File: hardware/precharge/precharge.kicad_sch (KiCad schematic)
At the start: 14 parts

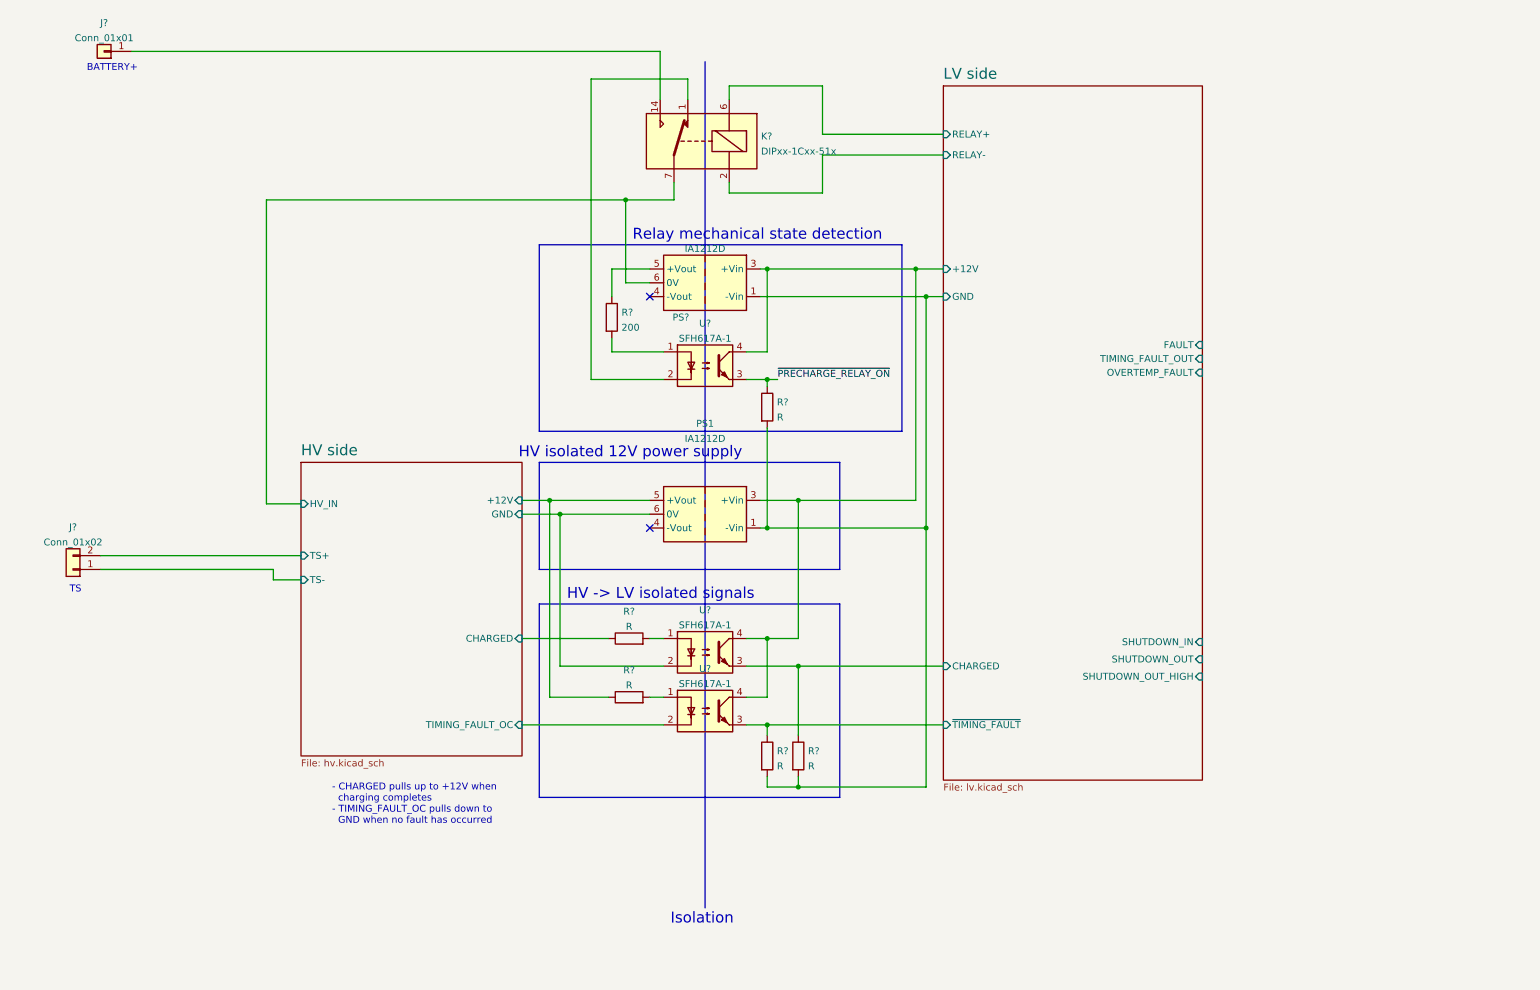
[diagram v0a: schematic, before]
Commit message: Added part numbers for most components, added LEDs, tweaked LV side.
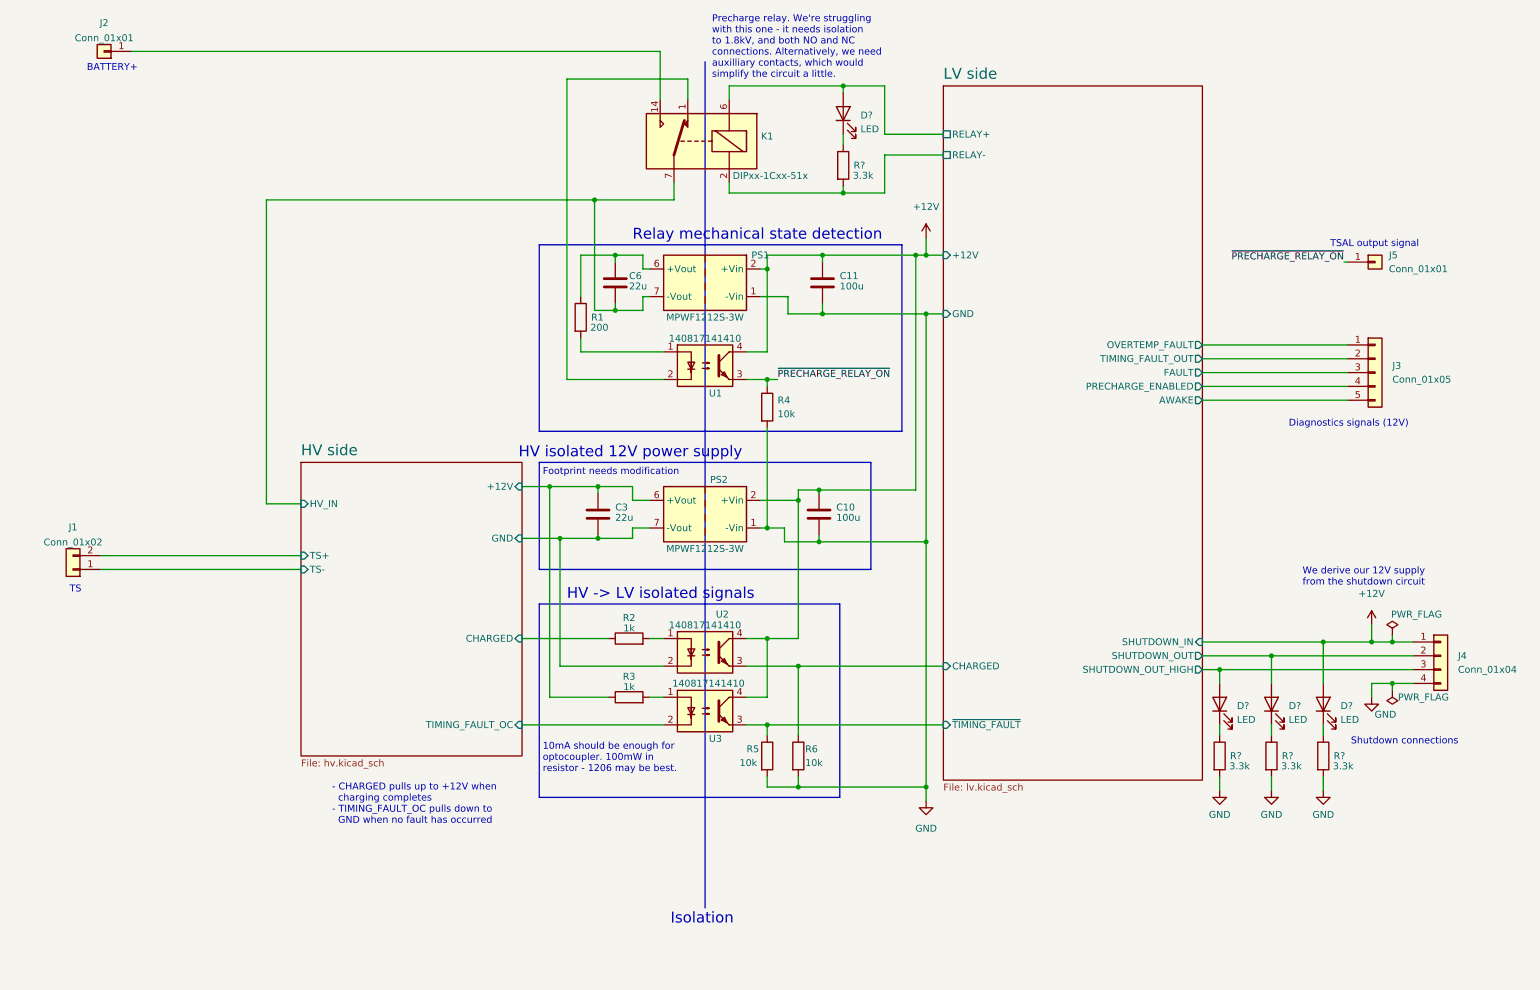
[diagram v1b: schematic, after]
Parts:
- removed PS1, PS?: IA1212D, Converter_DCDC:Converter_DCDC_XP_POWER-IAxxxxD_THT, symbol Converter_DCDC:IA1212D
- added C10, C11: 100u, symbol Device:C
- added C3, C6: 22u, symbol Device:C
- added D? (x4): LED, symbol Device:LED
- added J3: Conn_01x05, symbol Connector_Generic:Conn_01x05
- added J4: Conn_01x04, symbol Connector_Generic:Conn_01x04
- added J5: Conn_01x01, symbol Connector_Generic:Conn_01x01
- added PS1, PS2: MPWF1212S-3W, Converter_DCDC:Converter_DCDC_XP_POWER-ITXxxxxSA_THT, symbol Converter_DCDC:ITX1212SA
- added R? (x4): 3.3k, symbol Device:R
- R2, R3: renamed from R?; value R -> 1k
- R4, R5, R6: renamed from R?; value R -> 10k
- U1, U2, U3: renamed from U?; value SFH617A-1 -> 140817141410
- gave numbers to parts that had none: 4
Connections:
- net HV side/+12V: now also C3.2, PS2.6 (+Vout)
- net HV side/GND: now also C3.1, PS2.7 (-Vout)
- net HV side/HV_IN: now also C6.1, PS1.7 (-Vout)
- net LV side/FAULT: now also J3.3 (Pin_3)
- net LV side/OVERTEMP_FAULT: now also J3.1 (Pin_1)
- net LV side/RELAY+: now also D?.2 (A)
- net LV side/RELAY-: now also R?.2
- net LV side/SHUTDOWN_OUT: now also D?.2 (A), J4.2 (Pin_2)
- net LV side/SHUTDOWN_OUT_HIGH: now also D?.2 (A), J4.3 (Pin_3)
- net LV side/TIMING_FAULT_OUT: now also J3.2 (Pin_2)
- net ~{PRECHARGE_RELAY_ON}: now also J5.1 (Pin_1)
- net at R1.1: now also C6.2, PS1.6 (+Vout)
- net LV side/+12V renamed +12V
- net +12V: now also C10.2, C11.2, D?.2 (A), J4.1 (Pin_1), PS1.2 (+Vin), PS2.2 (+Vin)
- net LV side/GND renamed GND
- net GND: now also C10.1, C11.1, J4.4 (Pin_4), PS1.1 (-Vin), PS2.1 (-Vin), R?.2, R?.2, R?.2
- new net: D?.1 (K), R?.1 (x4)
- new net LV side/AWAKE: J3.5 (Pin_5)
- new net LV side/PRECHARGE_ENABLED: J3.4 (Pin_4)
- no-connect marks 2 -> 0
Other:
- sheet LV side ports: added AWAKE, PRECHARGE_ENABLED; removed none
- note added: "10mA should be enough for optocoupler. 100mW in resistor - 1206 may be best."
- note added: "Diagnostics signals (12V)"
- note added: "Footprint needs modification"
- note added: "Precharge relay. We're struggling with this one - it needs isolation to 1.8kV, and both NO and NC connections. Alternatively, we need auxilliary contacts, which would simplify the circuit a little."
- note added: "Shutdown connections"
- note added: "TSAL output signal"
- note added: "We derive our 12V supply from the shutdown circuit"
- moved on the sheet: R1

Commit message: Tweaks, nearly done
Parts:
- added C?: 100u, symbol Device:C
- added D?: SS14+, symbol Device:D
- R1: value 200 -> 1k
- gave numbers to parts that had none: 8
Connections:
- net HV side/CHARGED is gone; now on net HV side/+12V: R2.1
- net HV side/TIMING_FAULT_OC is gone; now on net HV side/GND: U3.2
- net +12V: now also C?.1, D?.1 (K); no longer D12.2 (A), J4.1 (Pin_1)
- net GND: now also C?.2
- net HV side/+12V: now also R3.2; no longer R3.1
- net HV side/GND: no longer U2.2
- net HV side/~{TIMING_FAULT_OC}: now reaches U3.1
- net HV side/~{TIMING_FAULT_OC}: now also R3.1; no longer R3.2
- new net HV side/~{CHARGED}: U2.2
- new net LV side/SHUTDOWN_IN: D12.2 (A), D?.2 (A), J4.1 (Pin_1)
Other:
- sheet HV side ports: added ~{CHARGED}, ~{TIMING_FAULT_OC}; removed CHARGED, TIMING_FAULT_OC
- note added: "Still to do: - Find precharge relay - Choose connectors - Assign / create footprints - Create BOM, source components - Layout PCB"
- note added: "The 12V supply is derived from the shutdown circuit, via a diode to prevent the capacitors from keeping the AIRs on once the shutdown circuit opens."
- note added: "~{TIMING_FAULT_OC} pulls low if a fault occurs, cutting off the optocoupler and signalling an error."
- note removed: "- CHARGED pulls up to +12V when charging completes - TIMING_FAULT_OC pulls down to GND when no fault has occurred"
- note removed: "We derive our 12V supply from the shutdown circuit"
- moved on the sheet: C10, C11, C3, C6, D10, D11, D12, D9, J1, J2, J3, J4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

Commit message: Assigned some footprints, created footprint library
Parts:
- removed C10, C11: 100u, symbol Device:C
- removed C3, C6: 22u, symbol Device:C
- added C10, C11: 100u, Capacitor_THT:CP_Radial_D8.0mm_P3.50mm, symbol Device:C_Polarized
- added C3, C6: 22u, Capacitor_THT:CP_Radial_D8.0mm_P3.50mm, symbol Device:C_Polarized
- C13: renamed from C?; footprint (none) -> Capacitor_THT:CP_Radial_D8.0mm_P3.50mm
- D1: renamed from D?; footprint (none) -> Diode_SMD:D_SMA
- D10, D11, D12, D9: footprint (none) -> LED_SMD:LED_0603_1608Metric
- PS2: footprint Converter_DCDC:Converter_DCDC_XP_POWER-ITXxxxxSA_THT -> footprints:MPWF1212S-3W
- R1, R2, R3, R4, R41, R42, R43, R44, R5, R6: footprint (none) -> Resistor_SMD:R_0603_1608Metric
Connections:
- net +12V: now also C10.1, C11.1
- net GND: now also C10.2, C11.2
- net HV side/+12V: now also C3.1
- net HV side/GND: now also C3.2
- net HV side/HV_IN: now also C6.2
- net at PS1.6 (+Vout), R1.1: now also C6.1

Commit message: Preliminary PCB placement
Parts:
- removed C13: 100u, Capacitor_THT:CP_Radial_D8.0mm_P3.50mm, symbol Device:C
- added C1: 100u, Capacitor_THT:CP_Radial_D6.3mm_P2.50mm, symbol Device:C_Polarized
- C10, C11: footprint Capacitor_THT:CP_Radial_D8.0mm_P3.50mm -> Capacitor_THT:CP_Radial_D6.3mm_P2.50mm
- J1: footprint (none) -> Connector_PinHeader_2.54mm:PinHeader_1x02_P2.54mm_Horizontal
- J2, J5: footprint (none) -> Connector_PinHeader_2.54mm:PinHeader_1x01_P2.54mm_Horizontal
- J3: footprint (none) -> Connector_PinHeader_2.54mm:PinHeader_1x05_P2.54mm_Horizontal
- J4: footprint (none) -> Connector_PinHeader_2.54mm:PinHeader_1x04_P2.54mm_Horizontal
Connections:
- net +12V: now also C1.1
- net GND: now also C1.2
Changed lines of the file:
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@@
       (effects (font (size 1.27 1.27)) (justify left))
     )
-    (property "Footprint" "Capacitor_THT:CP_Radial_D8.0mm_P3.50mm" (id 2) (at 139.3952 109.855 0)
+    (property "Footprint" "Capacitor_THT:CP_Radial_D6.3mm_P2.50mm" (id 2) (at 139.3952 109.855 0)
       (effects (font (size 1.27 1.27)) hide)
     )
@@
       (effects (font (size 1.27 1.27)) (justify left))
     )
-    (property "Footprint" "" (id 2) (at 240.665 59.69 0)
+    (property "Footprint" "Connector_PinHeader_2.54mm:PinHeader_1x01_P2.54mm_Horizontal" (id 2) (at 240.665 59.69 0)
       (effects (font (size 1.27 1.27)) hide)
     )
@@
       (effects (font (size 1.27 1.27)) (justify left))
     )
-    (property "Footprint" "" (id 2) (at 240.665 80.01 0)
+    (property "Footprint" "Connector_PinHeader_2.54mm:PinHeader_1x05_P2.54mm_Horizontal" (id 2) (at 240.665 80.01 0)
       (effects (font (size 1.27 1.27)) hide)
     )
@@
     (pin "2")
   )
-  (symbol (lib_id "Device:C") (at 249.555 121.92 0) (unit 1)
-    (in_bom yes) (on_board yes) (fields_autoplaced)
-    (property "Reference" "C13" (id 0) (at 252.73 120.6499 0)
-      (effects (font (size 1.27 1.27)) (justify left))
-    )
-    (property "Value" "100u" (id 1) (at 252.73 123.1899 0)
-      (effects (font (size 1.27 1.27)) (justify left))
-    )
-    (property "Footprint" "Capacitor_THT:CP_Radial_D8.0mm_P3.50mm" (id 2) (at 250.5202 125.73 0)
-      (effects (font (size 1.27 1.27)) hide)
-    )
-    (property "Datasheet" "~" (id 3) (at 249.555 121.92 0)
-      (effects (font (size 1.27 1.27)) hide)
-    )
-    (pin "1")
-    (pin "2")
-  )
   (symbol (lib_id "Device:R") (at 128.905 86.36 0) (unit 1)
     (in_bom yes) (on_board yes) (fields_autoplaced)
@@
       (effects (font (size 1.27 1.27)) (justify left))
     )
-    (property "Footprint" "" (id 2) (at 269.24 132.08 0)
+    (property "Footprint" "Connector_PinHeader_2.54mm:PinHeader_1x04_P2.54mm_Horizontal" (id 2) (at 269.24 132.08 0)
       (effects (font (size 1.27 1.27)) hide)
     )
@@
     (property "Reference" "J2" (id 0) (at 28.575 15.7185 0))
     (property "Value" "Conn_01x01" (id 1) (at 28.575 18.4936 0))
-    (property "Footprint" "" (id 2) (at 28.575 20.955 0)
+    (property "Footprint" "Connector_PinHeader_2.54mm:PinHeader_1x01_P2.54mm_Horizontal" (id 2) (at 28.575 20.955 0)
       (effects (font (size 1.27 1.27)) hide)
     )
@@
     (property "Reference" "J1" (id 0) (at 26.035 108.4285 0))
     (property "Value" "Conn_01x02" (id 1) (at 26.035 111.2036 0))
-    (property "Footprint" "" (id 2) (at 26.035 116.205 0)
+    (property "Footprint" "Connector_PinHeader_2.54mm:PinHeader_1x02_P2.54mm_Horizontal" (id 2) (at 26.035 116.205 0)
       (effects (font (size 1.27 1.27)) hide)
     )
@@
       (effects (font (size 1.27 1.27)) (justify left))
     )
-    (property "Footprint" "Capacitor_THT:CP_Radial_D8.0mm_P3.50mm" (id 2) (at 140.0302 67.31 0)
+    (property "Footprint" "Capacitor_THT:CP_Radial_D6.3mm_P2.50mm" (id 2) (at 140.0302 67.31 0)
       (effects (font (size 1.27 1.27)) hide)
     )
@@
     )
     (property "Datasheet" "~" (id 3) (at 231.14 140.97 0)
+      (effects (font (size 1.27 1.27)) hide)
+    )
+    (pin "1")
+    (pin "2")
+  )
+  (symbol (lib_id "Device:C_Polarized") (at 249.555 121.92 0) (unit 1)
+    (in_bom yes) (on_board yes) (fields_autoplaced)
+    (property "Reference" "C1" (id 0) (at 253.365 119.7609 0)
+      (effects (font (size 1.27 1.27)) (justify left))
+    )
+    (property "Value" "100u" (id 1) (at 253.365 122.3009 0)
+      (effects (font (size 1.27 1.27)) (justify left))
+    )
+    (property "Footprint" "Capacitor_THT:CP_Radial_D6.3mm_P2.50mm" (id 2) (at 250.5202 125.73 0)
+      (effects (font (size 1.27 1.27)) hide)
+    )
+    (property "Datasheet" "~" (id 3) (at 249.555 121.92 0)
       (effects (font (size 1.27 1.27)) hide)
     )
@@
       (reference "#PWR0103") (unit 1) (value "GND") (footprint "")
     )
-    (path "/86ebb052-21e6-4e49-945d-049a70338ab6/7bb00e99-dcca-4cb6-9153-ec6413060b21"
-      (reference "C1") (unit 1) (value "10u") (footprint "Capacitor_SMD:C_0805_2012Metric")
-    )
-    (path "/86ebb052-21e6-4e49-945d-049a70338ab6/d9ab0181-4626-44cd-8652-4df63090dfd7"
-      (reference "C2") (unit 1) (value "3.3u") (footprint "Capacitor_SMD:C_0805_2012Metric")
+    (path "/d07b04ce-e928-40b9-a472-6bd933c4ab15"
+      (reference "C1") (unit 1) (value "100u") (footprint "Capacitor_THT:CP_Radial_D6.3mm_P2.50mm")
+    )
+    (path "/86ebb052-21e6-4e49-945d-049a70338ab6/eb341917-c9ac-4a7f-abc5-9def26d9d22c"
+      (reference "C2") (unit 1) (value "10u") (footprint "Capacitor_THT:CP_Radial_D5.0mm_P2.00mm")
     )
     (path "/99b2acd7-7e4c-4d3b-bdd2-58e4013cdd30"
       (reference "C3") (unit 1) (value "22u") (footprint "Capacitor_THT:CP_Radial_D8.0mm_P3.50mm")
     )
-    (path "/a25b3faf-d95a-49ad-9b40-7c3f8d869233/30ff122b-721a-44e9-9b9d-bafb6992875a"
-      (reference "C4") (unit 1) (value "4.7u") (footprint "Capacitor_SMD:C_0805_2012Metric")
+    (path "/86ebb052-21e6-4e49-945d-049a70338ab6/c4c1bec5-1dcf-436d-b0f6-b11b14e3cb89"
+      (reference "C4") (unit 1) (value "3.3u") (footprint "Capacitor_THT:CP_Radial_D5.0mm_P2.00mm")
     )
     (path "/a25b3faf-d95a-49ad-9b40-7c3f8d869233/4f12e04b-1a72-4b55-bb85-71631b67cbb9"
@@
     )
     (path "/06389b60-1f88-4cef-9de0-a10ad569e8a2"
-      (reference "C10") (unit 1) (value "100u") (footprint "Capacitor_THT:CP_Radial_D8.0mm_P3.50mm")
+      (reference "C10") (unit 1) (value "100u") (footprint "Capacitor_THT:CP_Radial_D6.3mm_P2.50mm")
     )
     (path "/c4c78c02-48ba-4d62-ba5a-1ad4c0381616"
-      (reference "C11") (unit 1) (value "100u") (footprint "Capacitor_THT:CP_Radial_D8.0mm_P3.50mm")
+      (reference "C11") (unit 1) (value "100u") (footprint "Capacitor_THT:CP_Radial_D6.3mm_P2.50mm")
     )
     (path "/86ebb052-21e6-4e49-945d-049a70338ab6/06978fec-2c88-4699-ae0a-45bd99ddbe49"
       (reference "C12") (unit 1) (value "100n") (footprint "Capacitor_SMD:C_0603_1608Metric")
     )
-    (path "/5a4903ab-34f6-4f97-86ad-22f7d4094299"
-      (reference "C13") (unit 1) (value "100u") (footprint "Capacitor_THT:CP_Radial_D8.0mm_P3.50mm")
+    (path "/a25b3faf-d95a-49ad-9b40-7c3f8d869233/d17a13fe-7293-4b27-9cb1-10ec5351ae00"
+      (reference "C13") (unit 1) (value "4.7u") (footprint "Capacitor_THT:CP_Radial_D5.0mm_P2.00mm")
     )
     (path "/71f2e601-ac09-4765-9de5-403d309d97b5"
@@
     )
     (path "/86ebb052-21e6-4e49-945d-049a70338ab6/9701a355-0600-47c8-8807-3e75f65e00ef"
-      (reference "F1") (unit 1) (value "Fuse") (footprint "")
+      (reference "F1") (unit 1) (value "Fuse") (footprint "footprints:fuseholder")
     )
     (path "/c1d028f3-91e9-41f8-8563-411af756b606"
-      (reference "J1") (unit 1) (value "Conn_01x02") (footprint "")
+      (reference "J1") (unit 1) (value "Conn_01x02") (footprint "Connector_PinHeader_2.54mm:PinHeader_1x02_P2.54mm_Horizontal")
     )
     (path "/9675ae6d-9635-4b89-ab4f-854f5484396b"
-      (reference "J2") (unit 1) (value "Conn_01x01") (footprint "")
+      (reference "J2") (unit 1) (value "Conn_01x01") (footprint "Connector_PinHeader_2.54mm:PinHeader_1x01_P2.54mm_Horizontal")
     )
     (path "/48a360c2-dee0-4abf-adcb-faab1191a5cc"
-      (reference "J3") (unit 1) (value "Conn_01x05") (footprint "")
+      (reference "J3") (unit 1) (value "Conn_01x05") (footprint "Connector_PinHeader_2.54mm:PinHeader_1x05_P2.54mm_Horizontal")
     )
     (path "/616c1ff6-bb93-43c9-a485-6175455d841d"
-      (reference "J4") (unit 1) (value "Conn_01x04") (footprint "")
+      (reference "J4") (unit 1) (value "Conn_01x04") (footprint "Connector_PinHeader_2.54mm:PinHeader_1x04_P2.54mm_Horizontal")
     )
     (path "/0e8f5783-8efb-4d69-a261-a2ad2e1cb0af"
-      (reference "J5") (unit 1) (value "Conn_01x01") (footprint "")
+      (reference "J5") (unit 1) (value "Conn_01x01") (footprint "Connector_PinHeader_2.54mm:PinHeader_1x01_P2.54mm_Horizontal")
     )
     (path "/b5366f00-a799-456a-9576-87bc4f5c10c9"
@@
     )
     (path "/a25b3faf-d95a-49ad-9b40-7c3f8d869233/0eaa663a-c98d-44db-8bf5-70ab2ac22caf"
-      (reference "K2") (unit 1) (value "G5Q-1") (footprint "Relay_THT:Relay_SPDT_Omron-G5Q-1")
+      (reference "K2") (unit 1) (value "G5Q-1EU DC12") (footprint "Relay_THT:Relay_SPDT_Omron-G5Q-1")
     )
     (path "/a25b3faf-d95a-49ad-9b40-7c3f8d869233/4e001036-2180-4366-a0f5-0b8745896e4b"
-      (reference "K3") (unit 1) (value "G5Q-1") (footprint "Relay_THT:Relay_SPDT_Omron-G5Q-1")
+      (reference "K3") (unit 1) (value "G5Q-1EU DC12") (footprint "Relay_THT:Relay_SPDT_Omron-G5Q-1")
     )
     (path "/86ebb052-21e6-4e49-945d-049a70338ab6/803c0043-b1c3-4bca-b4ae-77676bf2cde3"
@@
     )
     (path "/86ebb052-21e6-4e49-945d-049a70338ab6/0e0e2b56-1830-447b-9de6-a46355c5a1ff"
-      (reference "R25") (unit 1) (value "680") (footprint "Resistor_THT:R_Axial_Power_L75.0mm_W9.0mm_P86.36mm")
+      (reference "R25") (unit 1) (value "680") (footprint "footprints:HSA50680RJ")
     )
     (path "/86ebb052-21e6-4e49-945d-049a70338ab6/f99d9765-47b3-46d8-b421-2c5b27dab9dd"
